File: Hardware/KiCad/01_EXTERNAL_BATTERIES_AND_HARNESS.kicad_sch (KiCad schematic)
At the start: 0 parts

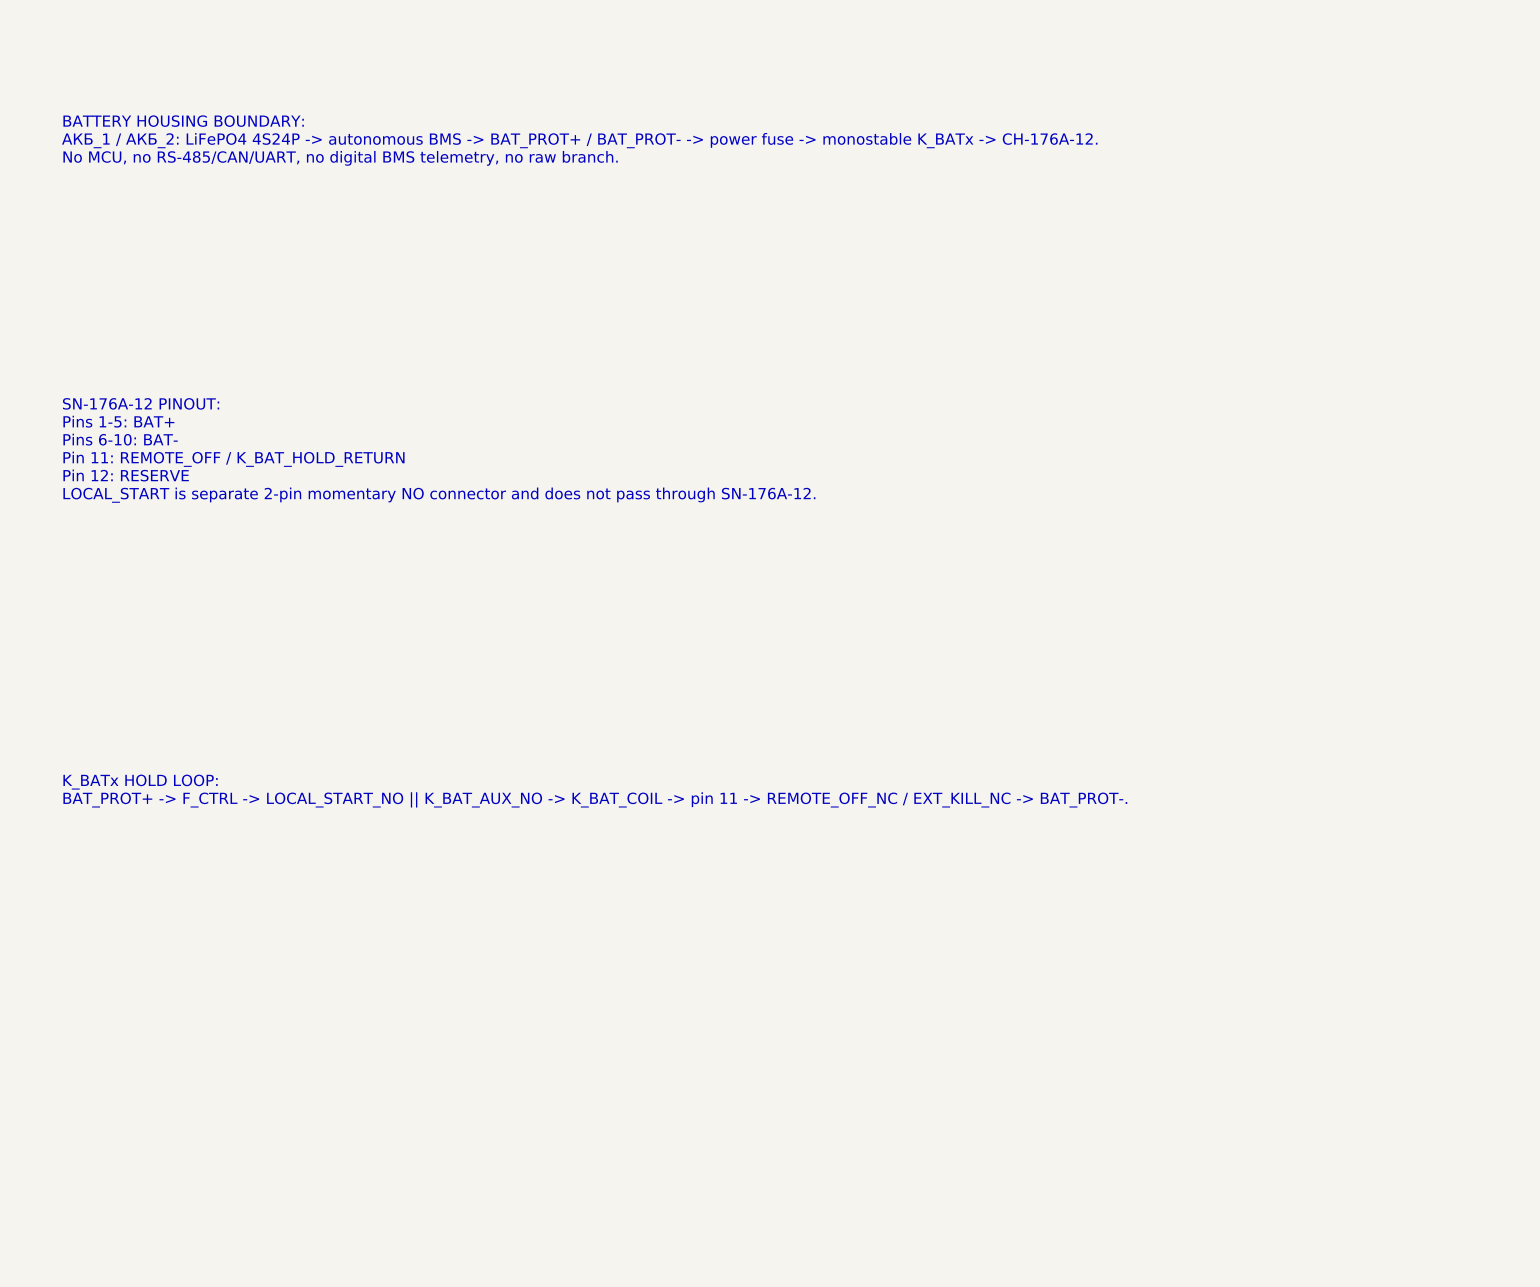
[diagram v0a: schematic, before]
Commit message: hardware: detail 01 external batteries and harness sheet
Translate 01_EXTERNAL_BATTERIES_AND_HARNESS into an Architecture Level A functional sheet.

Includes external battery housing boundaries, SN-176A-12 pinout, separate LOCAL_START, K_BATx hold-loop rules, and manifest update.

No component selection, footprints, or PCB layout.
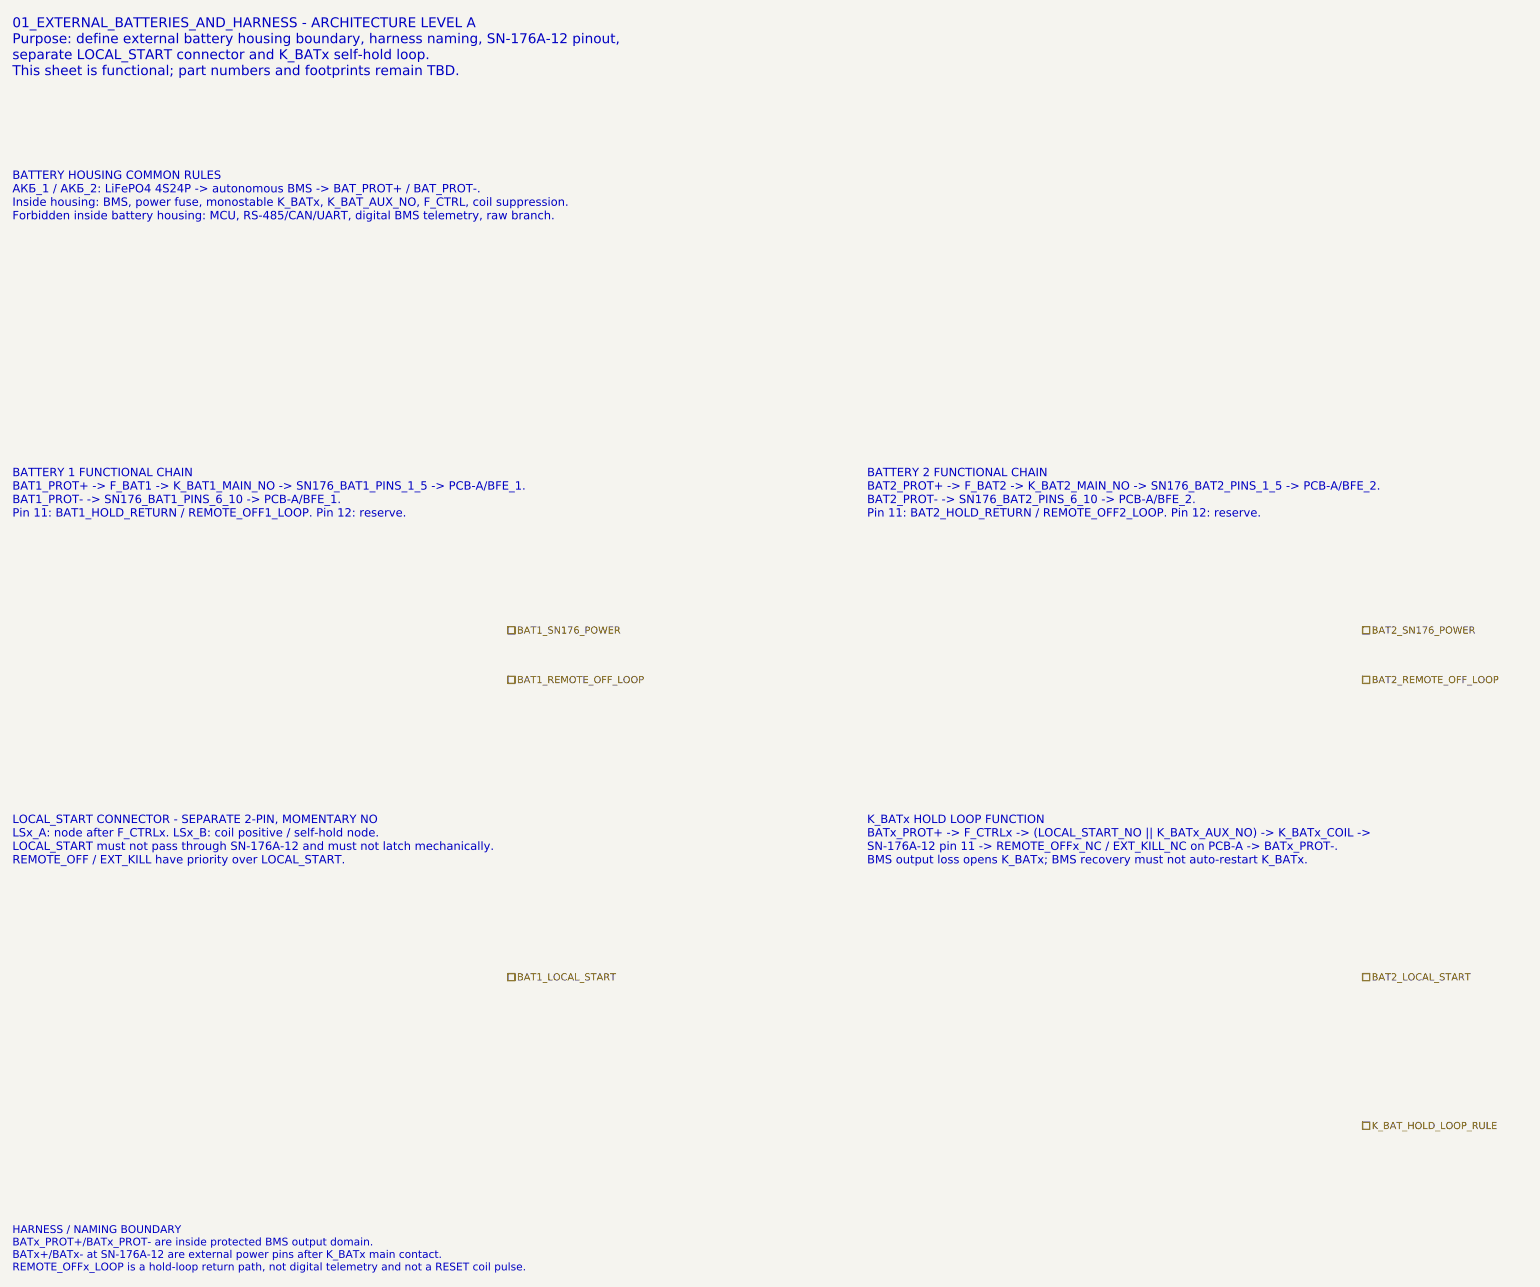
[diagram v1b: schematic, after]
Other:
- note added: "01_EXTERNAL_BATTERIES_AND_HARNESS - ARCHITECTURE LEVEL A Purpose: define external battery housing boundary, harness naming, SN-176A-12 pinout, separate LOCAL_START connector and K_BATx self-hold loop. This sheet is functional; part numbers and footprints remain TBD."
- note added: "BATTERY 1 FUNCTIONAL CHAIN BAT1_PROT+ -> F_BAT1 -> K_BAT1_MAIN_NO -> SN176_BAT1_PINS_1_5 -> PCB-A/BFE_1. BAT1_PROT- -> SN176_BAT1_PINS_6_10 -> PCB-A/BFE_1. Pin 11: BAT1_HOLD_RETURN / REMOTE_OFF1_LOOP. Pin 12: reserve."
- note added: "BATTERY 2 FUNCTIONAL CHAIN BAT2_PROT+ -> F_BAT2 -> K_BAT2_MAIN_NO -> SN176_BAT2_PINS_1_5 -> PCB-A/BFE_2. BAT2_PROT- -> SN176_BAT2_PINS_6_10 -> PCB-A/BFE_2. Pin 11: BAT2_HOLD_RETURN / REMOTE_OFF2_LOOP. Pin 12: reserve."
- note added: "BATTERY HOUSING COMMON RULES АКБ_1 / АКБ_2: LiFePO4 4S24P -> autonomous BMS -> BAT_PROT+ / BAT_PROT-. Inside housing: BMS, power fuse, monostable K_BATx, K_BAT_AUX_NO, F_CTRL, coil suppression. Forbidden inside battery housing: MCU, RS-485/CAN/UART, digital BMS telemetry, raw branch."
- note added: "HARNESS / NAMING BOUNDARY BATx_PROT+/BATx_PROT- are inside protected BMS output domain. BATx+/BATx- at SN-176A-12 are external power pins after K_BATx main contact. REMOTE_OFFx_LOOP is a hold-loop return path, not digital telemetry and not a RESET coil pulse."
- note added: "K_BATx HOLD LOOP FUNCTION BATx_PROT+ -> F_CTRLx -> (LOCAL_START_NO || K_BATx_AUX_NO) -> K_BATx_COIL -> SN-176A-12 pin 11 -> REMOTE_OFFx_NC / EXT_KILL_NC on PCB-A -> BATx_PROT-. BMS output loss opens K_BATx; BMS recovery must not auto-restart K_BATx."
- note added: "LOCAL_START CONNECTOR - SEPARATE 2-PIN, MOMENTARY NO LSx_A: node after F_CTRLx. LSx_B: coil positive / self-hold node. LOCAL_START must not pass through SN-176A-12 and must not latch mechanically. REMOTE_OFF / EXT_KILL have priority over LOCAL_START."
- note removed: "BATTERY HOUSING BOUNDARY: АКБ_1 / АКБ_2: LiFePO4 4S24P -> autonomous BMS -> BAT_PROT+ / BAT_PROT- -> power fuse -> monostable K_BATx -> СН-176А-12. No MCU, no RS-485/CAN/UART, no digital BMS telemetry, no raw branch."
- note removed: "K_BATx HOLD LOOP: BAT_PROT+ -> F_CTRL -> LOCAL_START_NO || K_BAT_AUX_NO -> K_BAT_COIL -> pin 11 -> REMOTE_OFF_NC / EXT_KILL_NC -> BAT_PROT-."
- note removed: "SN-176A-12 PINOUT: Pins 1-5: BAT+ Pins 6-10: BAT- Pin 11: REMOTE_OFF / K_BAT_HOLD_RETURN Pin 12: RESERVE LOCAL_START is separate 2-pin momentary NO connector and does not pass through SN-176A-12."
- company: (none) -> Gonoboben/plataVM
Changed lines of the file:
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@@
 	(title_block
 		(title "01_EXTERNAL_BATTERIES_AND_HARNESS")
-		(date "2026-07-14")
-		(rev "A0")
-		(comment 1 "External battery housings and harness boundaries")
+		(date "2026-07-15")
+		(rev "A1")
+		(company "Gonoboben/plataVM")
+		(comment 1 "External battery housings, SN-176A-12, LOCAL_START and K_BATx hold-loop")
+		(comment 2 "No contactor model, fuse rating, suppressor or connector family selected here")
 	)
-	(text "SN-176A-12 PINOUT:\nPins 1-5: BAT+\nPins 6-10: BAT-\nPin 11: REMOTE_OFF / K_BAT_HOLD_RETURN\nPin 12: RESERVE\nLOCAL_START is separate 2-pin momentary NO connector and does not pass through SN-176A-12."
+	(text "01_EXTERNAL_BATTERIES_AND_HARNESS - ARCHITECTURE LEVEL A\nPurpose: define external battery housing boundary, harness naming, SN-176A-12 pinout,\nseparate LOCAL_START connector and K_BATx self-hold loop.\nThis sheet is functional; part numbers and footprints remain TBD."
 		(exclude_from_sim no)
-		(at 20 75 0)
+		(at 12 10 0)
 		(effects
 			(font
-				(size 1.8 1.8)
+				(size 1.6 1.6)
 			)
 			(justify left)
 		)
 	)
-	(text "BATTERY HOUSING BOUNDARY:\nАКБ_1 / АКБ_2: LiFePO4 4S24P -> autonomous BMS -> BAT_PROT+ / BAT_PROT- -> power fuse -> monostable K_BATx -> СН-176А-12.\nNo MCU, no RS-485/CAN/UART, no digital BMS telemetry, no raw branch."
+	(text "BATTERY HOUSING COMMON RULES\nАКБ_1 / АКБ_2: LiFePO4 4S24P -> autonomous BMS -> BAT_PROT+ / BAT_PROT-.\nInside housing: BMS, power fuse, monostable K_BATx, K_BAT_AUX_NO, F_CTRL, coil suppression.\nForbidden inside battery housing: MCU, RS-485/CAN/UART, digital BMS telemetry, raw branch."
 		(exclude_from_sim no)
-		(at 20 25 0)
+		(at 12 34 0)
 		(effects
 			(font
-				(size 1.8 1.8)
+				(size 1.35 1.35)
 			)
 			(justify left)
 		)
 	)
-	(text "K_BATx HOLD LOOP:\nBAT_PROT+ -> F_CTRL -> LOCAL_START_NO || K_BAT_AUX_NO -> K_BAT_COIL -> pin 11 -> REMOTE_OFF_NC / EXT_KILL_NC -> BAT_PROT-."
+	(text "BATTERY 1 FUNCTIONAL CHAIN\nBAT1_PROT+ -> F_BAT1 -> K_BAT1_MAIN_NO -> SN176_BAT1_PINS_1_5 -> PCB-A/BFE_1.\nBAT1_PROT- -> SN176_BAT1_PINS_6_10 -> PCB-A/BFE_1.\nPin 11: BAT1_HOLD_RETURN / REMOTE_OFF1_LOOP. Pin 12: reserve."
 		(exclude_from_sim no)
-		(at 20 130 0)
+		(at 12 82 0)
 		(effects
 			(font
-				(size 1.8 1.8)
+				(size 1.35 1.35)
 			)
 			(justify left)
+		)
+	)
+	(text "BATTERY 2 FUNCTIONAL CHAIN\nBAT2_PROT+ -> F_BAT2 -> K_BAT2_MAIN_NO -> SN176_BAT2_PINS_1_5 -> PCB-A/BFE_2.\nBAT2_PROT- -> SN176_BAT2_PINS_6_10 -> PCB-A/BFE_2.\nPin 11: BAT2_HOLD_RETURN / REMOTE_OFF2_LOOP. Pin 12: reserve."
+		(exclude_from_sim no)
+		(at 150 82 0)
+		(effects
+			(font
+				(size 1.35 1.35)
+			)
+			(justify left)
+		)
+	)
+	(text "LOCAL_START CONNECTOR - SEPARATE 2-PIN, MOMENTARY NO\nLSx_A: node after F_CTRLx. LSx_B: coil positive / self-hold node.\nLOCAL_START must not pass through SN-176A-12 and must not latch mechanically.\nREMOTE_OFF / EXT_KILL have priority over LOCAL_START."
+		(exclude_from_sim no)
+		(at 12 138 0)
+		(effects
+			(font
+				(size 1.35 1.35)
+			)
+			(justify left)
+		)
+	)
+	(text "K_BATx HOLD LOOP FUNCTION\nBATx_PROT+ -> F_CTRLx -> (LOCAL_START_NO || K_BATx_AUX_NO) -> K_BATx_COIL ->\nSN-176A-12 pin 11 -> REMOTE_OFFx_NC / EXT_KILL_NC on PCB-A -> BATx_PROT-.\nBMS output loss opens K_BATx; BMS recovery must not auto-restart K_BATx."
+		(exclude_from_sim no)
+		(at 150 138 0)
+		(effects
+			(font
+				(size 1.35 1.35)
+			)
+			(justify left)
+		)
+	)
+	(text "HARNESS / NAMING BOUNDARY\nBATx_PROT+/BATx_PROT- are inside protected BMS output domain.\nBATx+/BATx- at SN-176A-12 are external power pins after K_BATx main contact.\nREMOTE_OFFx_LOOP is a hold-loop return path, not digital telemetry and not a RESET coil pulse."
+		(exclude_from_sim no)
+		(at 12 204 0)
+		(effects
+			(font
+				(size 1.25 1.25)
+			)
+			(justify left)
+		)
+	)
+	(hierarchical_label "BAT1_SN176_POWER"
+		(shape passive)
+		(exclude_from_sim no)
+		(at 92 104 0)
+		(effects
+			(font
+				(size 1.15 1.15)
+			)
+			(justify left)
+		)
+	)
+	(hierarchical_label "BAT1_REMOTE_OFF_LOOP"
+		(shape passive)
+		(exclude_from_sim no)
+		(at 92 112 0)
+		(effects
+			(font
+				(size 1.15 1.15)
+			)
+			(justify left)
+		)
+	)
+	(hierarchical_label "BAT1_LOCAL_START"
+		(shape passive)
+		(exclude_from_sim no)
+		(at 92 160 0)
+		(effects
+			(font
+				(size 1.15 1.15)
+			)
+			(justify left)
+		)
+	)
+	(hierarchical_label "BAT2_SN176_POWER"
+		(shape passive)
+		(exclude_from_sim no)
+		(at 230 104 0)
+		(effects
+			(font
+				(size 1.15 1.15)
+			)
+			(justify left)
+		)
+	)
+	(hierarchical_label "BAT2_REMOTE_OFF_LOOP"
+		(shape passive)
+		(exclude_from_sim no)
+		(at 230 112 0)
+		(effects
+			(font
+				(size 1.15 1.15)
+			)
+			(justify left)
+		)
+	)
+	(hierarchical_label "BAT2_LOCAL_START"
+		(shape passive)
+		(exclude_from_sim no)
+		(at 230 160 0)
+		(effects
+			(font
+				(size 1.15 1.15)
+			)
+			(justify left)
+		)
+	)
+	(hierarchical_label "K_BAT_HOLD_LOOP_RULE"
+		(shape passive)
+		(exclude_from_sim no)
+		(at 230 184 0)
+		(effects
+			(font
+				(size 1.15 1.15)
+			)
+			(justify left)
